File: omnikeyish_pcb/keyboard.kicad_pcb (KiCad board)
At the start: 2 copper layers, 485.9 x 139.8 mm, 344 parts, among them SW1.1 KEY_P11, SW1.10 KEY_F6, SW1.11 KEY_F7, SW1.12 KEY_F8, SW1.13 KEY_F9, SW1.14 KEY_F10, SW1.15 KEY_F11, SW1.16 KEY_F12, SW1.17 KEY_PRINTSCREEN, SW1.18 KEY_SCROLL_LOCK, SW1.19 KEY_PAUSE, SW1.2 KEY_P12, SW1.20 KEY_VOLMUTE, SW1.21 KEY_VOLDOWN, SW1.22 KEY_VOLUP, SW1.23 KEY_POWER, SW1.3 KEY_ESCAPE, SW1.5 KEY_F1, SW1.6 KEY_F2, SW1.7 KEY_F3, SW1.8 KEY_F4, SW1.9 KEY_F5, SW1B.1 KEY_P11, SW1B.10 KEY_F6, SW1B.11 KEY_F7, SW1B.12 KEY_F8, SW1B.13 KEY_F9, SW1B.14 KEY_F10, SW1B.15 KEY_F11, SW1B.16 KEY_F12, SW1B.17 KEY_PRINTSCREEN, SW1B.18 KEY_SCROLL_LOCK, SW1B.19 KEY_PAUSE, SW1B.2 KEY_P12, SW1B.3 KEY_ESCAPE, SW1B.5 KEY_F1, SW1B.6 KEY_F2, SW1B.7 KEY_F3, SW1B.8 KEY_F4, SW1B.9 KEY_F5, SW1C.1 KEY_P11, SW1C.2 KEY_P12, SW1D.1 KEY_P11, SW1D.2 KEY_P12, SW2.1 KEY_P1, SW2.10 KEY_7, SW2.11 KEY_8, SW2.12 KEY_9, SW2.13 KEY_0, SW2.14 KEY_MINUS, SW2.15 KEY_EQUALS, SW2.16 KEY_BACKSPACE, SW2.17 KEY_INSERT, SW2.18 KEY_HOME, SW2.19 KEY_PGUP, SW2.2 KEY_P2, SW2.20 KEY_NUMLOCK, SW2.21 KEY_NUMDIVIDE, SW2.22 KEY_NUMTIMES, SW2.23 KEY_NUMMINUS, SW2.3 KEY_BACKQUOTE, SW2.4 KEY_1, SW2.5 KEY_2, SW2.6 KEY_3, SW2.7 KEY_4, SW2.8 KEY_5, SW2.9 KEY_6, SW2B.1 KEY_P1, SW2B.17 KEY_BIGINSERT, SW2B.2 KEY_P2, SW2C.1 KEY_P1, SW2C.2 KEY_P2, SW3.1 KEY_P3, SW3.10 KEY_U, SW3.11 KEY_I, SW3.12 KEY_O, SW3.13 KEY_P, SW3.14 KEY_LEFTBRACKET, SW3.15 KEY_RIGHTBRACKET, SW3.16 KEY_ANSIBACKSLASH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

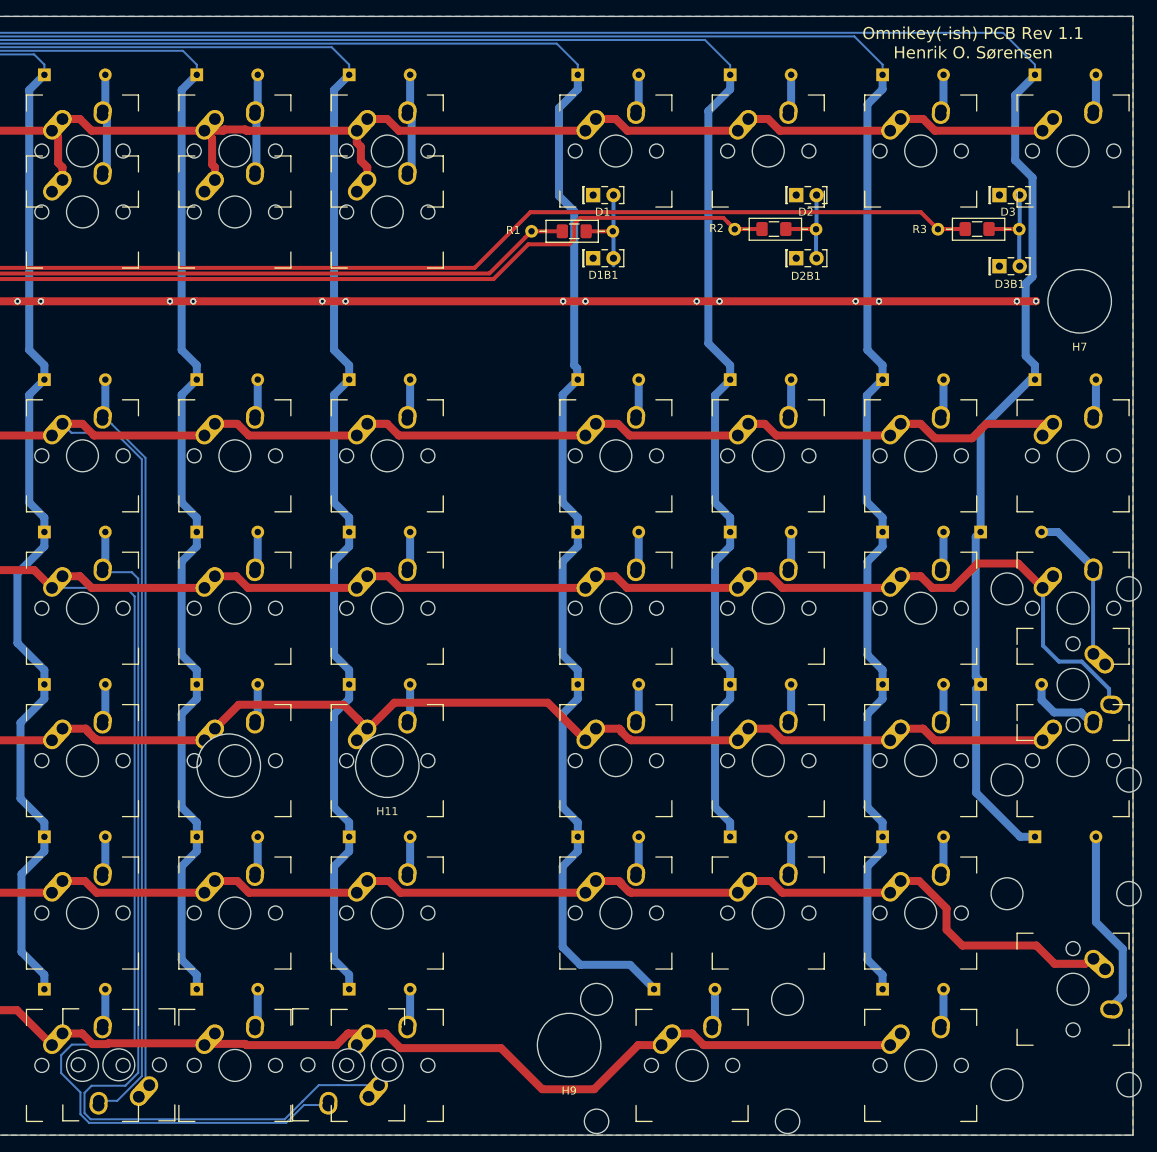
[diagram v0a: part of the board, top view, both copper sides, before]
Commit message: Rev 1.2: Fix brainfart matrix postion for Ultra's 1.5u insert and delete keys was wrong
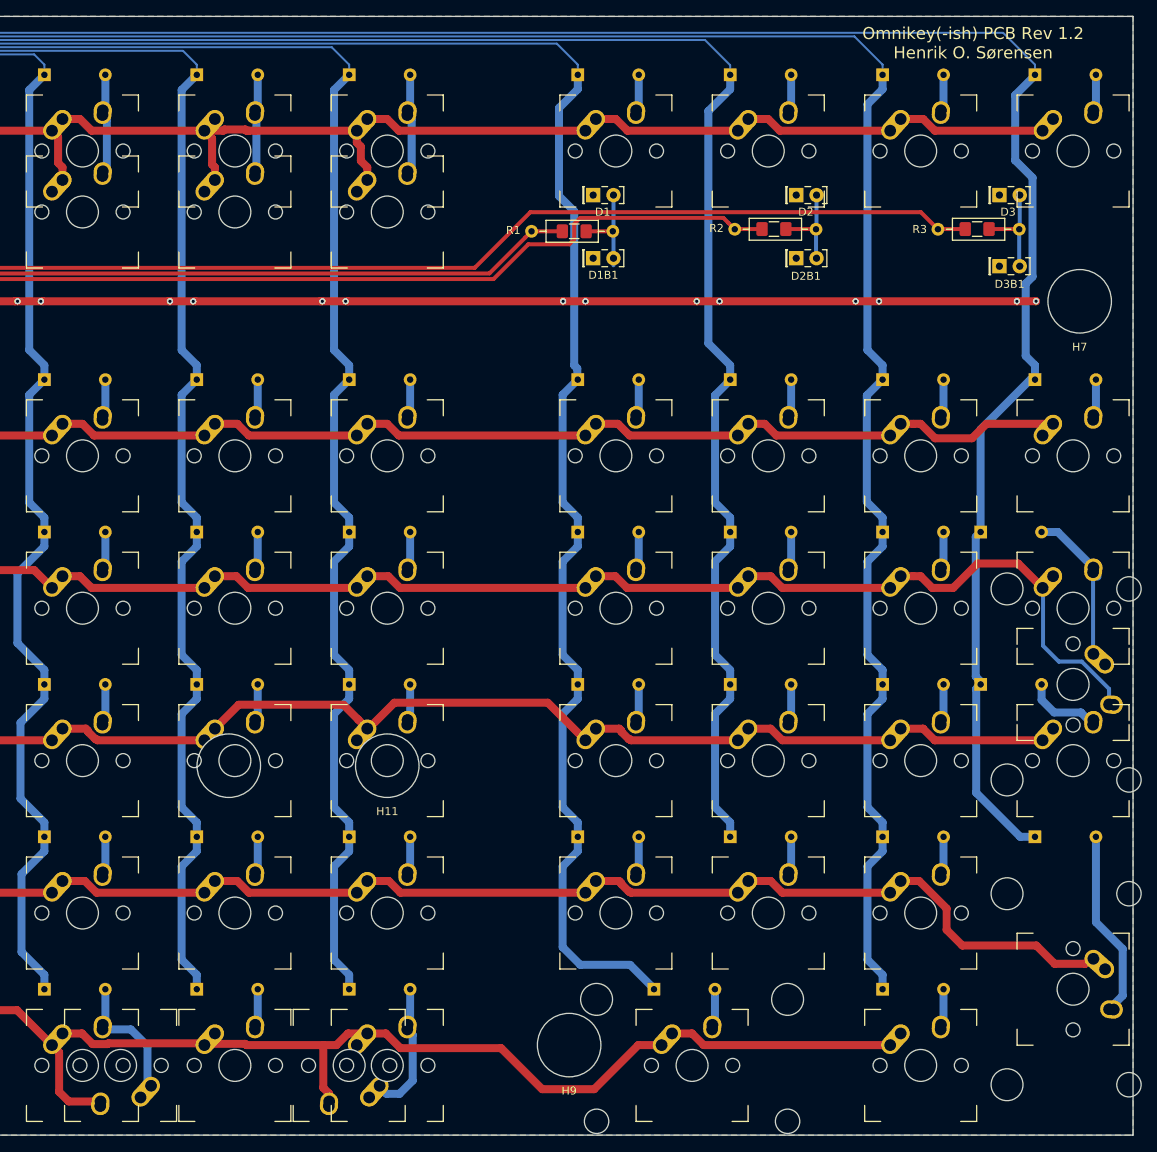
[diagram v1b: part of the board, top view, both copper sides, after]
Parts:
- removed SW2B.17: KEY_BIGINSERT, MX_Alps_Hybrid:MX-1.5U-NoLED
- removed SW3B.17: KEY_BIGDELETE, MX_Alps_Hybrid:MX-1.5U-NoLED
- added SW6B.17: KEY_ULTRAINSERT, MX_Alps_Hybrid:MX-1.5U-NoLED, F.Cu at (427.8, 174.0)
- added SW6B.19: KEY_ULTRADELETE, MX_Alps_Hybrid:MX-1.5U-NoLED, F.Cu at (456.4, 174.0)
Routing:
- net ROW3: track 786.9 -> 669.9 mm
- net Net-(D3.17-Pad2): track 120.4 -> 4.67 mm
- net ROW2: track 718.5 -> 623.0 mm
- net Net-(D2.17-Pad2): track 92.4 -> 4.67 mm
- net ROW6: track 767.6 -> 787.4 mm
- net Net-(D6.19-Pad2): track 5.17 -> 17.0 mm
- net Net-(D6.17-Pad2): track 5.17 -> 16.8 mm
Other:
- board text added: "Omnikey(-ish) PCB Rev 1.2 Henrik O. Sørensen"
- board text removed: "Omnikey(-ish) PCB Rev 1.1 Henrik O. Sørensen"

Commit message: Tweak silk screen location of 2u numpad plus
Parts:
- moved D4.23 0.65 mm to (534.7, 126.2)
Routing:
- net Net-(D4.3-Pad2): track 33.8 -> 29.6 mm
- net COL3: track 323.2 -> 324.2 mm
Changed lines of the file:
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@@
     (thickness 1.6)
     (drawings 50)
-    (tracks 2474)
+    (tracks 2473)
     (zones 0)
     (modules 344)
@@
   (module MX_Alps_Hybrid:MX-1.5U-NoLED (layer F.Cu)
     (at 456.3745 173.99 180)
-    (fp_text reference SW6B.19 (at 0 3.175) (layer B.SilkS)
+    (fp_text reference SW6B.19 (at -1.9685 -6.477) (layer B.SilkS)
       (effects (font (size 1 1) (thickness 0.15)) (justify mirror))
     )
@@
   (module MX_Alps_Hybrid:MX-1.5U-NoLED (layer F.Cu)
     (at 427.7995 173.99 180)
-    (fp_text reference SW6B.17 (at 0 3.175) (layer B.SilkS)
+    (fp_text reference SW6B.17 (at -2.8575 -6.35) (layer B.SilkS)
       (effects (font (size 1 1) (thickness 0.15)) (justify mirror))
     )
@@
   (module MX_Alps_Hybrid:MX-2U-NoLED (layer F.Cu)
     (at 546.862 126.365 270)
-    (fp_text reference SW3B.23 (at -1.7 -6.5 270) (layer B.SilkS)
+    (fp_text reference SW3B.23 (at -1.651 -6.35 270) (layer B.SilkS)
       (effects (font (size 1 1) (thickness 0.15)) (justify mirror))
     )
-    (fp_text value KEY_NUMBIGPLUS (at -0.2 -8.175 270) (layer B.SilkS)
+    (fp_text value KEY_NUMBIGPLUS (at -0.762 6.731 90) (layer B.SilkS)
       (effects (font (size 1 1) (thickness 0.15)) (justify mirror))
     )
@@
   )
   (module Diode_THT:D_DO-35_SOD27_P7.62mm_Horizontal (layer B.Cu)
-    (at 535.305 126.365)
+    (at 534.67 126.238)
     (descr "Diode, DO-35_SOD27 series, Axial, Horizontal, pin pitch=7.62mm, , length*diameter=4*2mm^2, , http://www.diodes.com/_files/packages/DO-35.pdf")
     (tags "Diode DO-35_SOD27 series Axial Horizontal pin pitch 7.62mm  length 4mm diameter 2mm")
-    (fp_text reference D4.23 (at 4.191 -2.286) (layer B.SilkS)
+    (fp_text reference D4.23 (at -2.032 0.127 90) (layer B.SilkS)
       (effects (font (size 1 1) (thickness 0.15)) (justify mirror))
     )
@@
   (module MX_Alps_Hybrid:MX-1U-NoLED (layer F.Cu)
     (at 546.862 116.84)
-    (fp_text reference SW3.23 (at -0.05 -7.075) (layer B.SilkS)
+    (fp_text reference SW3.23 (at 0 -8.636) (layer B.SilkS)
       (effects (font (size 1 1) (thickness 0.15)) (justify mirror))
     )
-    (fp_text value KEY_NUMPLUS (at 0 2.875) (layer B.SilkS)
+    (fp_text value KEY_NUMPLUS (at -0.381 -7.112) (layer B.SilkS)
       (effects (font (size 1 1) (thickness 0.15)) (justify mirror))
     )
@@
   (segment (start 126.873 145.415) (end 122.301 149.987) (width 1) (layer B.Cu) (net 21))
   (segment (start 127.762 145.415) (end 126.873 145.415) (width 1) (layer B.Cu) (net 21))
-  (segment (start 122.9995 140.6525) (end 127.762 145.415) (width 1) (layer B.Cu) (net 21))
-  (segment (start 122.9995 131.1275) (end 122.9995 140.6525) (width 1) (layer B.Cu) (net 21))
-  (segment (start 127.762 126.365) (end 122.9995 131.1275) (width 1) (layer B.Cu) (net 21))
   (segment (start 124.194978 46.747022) (end 120.777 50.165) (width 0.25) (layer F.Cu) (net 21))
   (segment (start 279.146 71.755) (end 280.242033 70.658967) (width 0.25) (layer F.Cu) (net 21))
@@
   (segment (start 280.242033 49.221979) (end 277.767076 46.747022) (width 0.25) (layer F.Cu) (net 21))
   (segment (start 277.767076 46.747022) (end 124.194978 46.747022) (width 0.25) (layer F.Cu) (net 21))
+  (segment (start 121.793 139.446) (end 127.762 145.415) (width 1) (layer B.Cu) (net 21))
+  (segment (start 121.793 132.334) (end 121.793 139.446) (width 1) (layer B.Cu) (net 21))
+  (segment (start 127.762 126.365) (end 121.793 132.334) (width 1) (layer B.Cu) (net 21))
   (segment (start 225.8695 50.165) (end 225.8695 54.8325) (width 1) (layer B.Cu) (net 22))
   (segment (start 209.931 62.23) (end 206.502 62.23) (width 1) (layer B.Cu) (net 22))
@@
   (segment (start 72.1995 90.065) (end 70.0405 92.224) (width 1) (layer B.Cu) (net 24))
   (segment (start 72.1995 88.265) (end 72.1995 90.065) (width 1) (layer B.Cu) (net 24))
-  (segment (start 70.0405 84.306) (end 72.1995 86.465) (width 1) (layer B.Cu) (net 24))
-  (segment (start 70.0405 54.124) (end 70.0405 84.306) (width 1) (layer B.Cu) (net 24))
-  (segment (start 72.1995 51.965) (end 70.0405 54.124) (width 1) (layer B.Cu) (net 24))
+  (segment (start 69.596 83.8615) (end 72.1995 86.465) (width 1) (layer B.Cu) (net 24))
+  (segment (start 69.596 54.5685) (end 69.596 83.8615) (width 1) (layer B.Cu) (net 24))
+  (segment (start 72.1995 51.965) (end 69.596 54.5685) (width 1) (layer B.Cu) (net 24))
   (segment (start 72.1995 86.465) (end 72.1995 88.265) (width 1) (layer B.Cu) (net 24))
   (segment (start 72.1995 50.165) (end 72.1995 51.965) (width 1) (layer B.Cu) (net 24))
@@
   (segment (start 135.382 130.4925) (end 135.0645 130.81) (width 1) (layer B.Cu) (net 63))
   (segment (start 135.382 126.365) (end 135.382 130.4925) (width 1) (layer B.Cu) (net 63))
-  (segment (start 137.50075 130.865) (end 137.44575 130.81) (width 1) (layer B.Cu) (net 63))
-  (segment (start 139.237 130.865) (end 137.50075 130.865) (width 1) (layer B.Cu) (net 63))
-  (segment (start 138.037 141.865) (end 142.037 137.865) (width 1) (layer B.Cu) (net 63))
-  (segment (start 142.037 137.865) (end 142.037 133.665) (width 1) (layer B.Cu) (net 63))
-  (segment (start 142.037 133.665) (end 139.237 130.865) (width 1) (layer B.Cu) (net 63))
-  (segment (start 129.11825 141.865) (end 138.037 141.865) (width 1) (layer B.Cu) (net 63))
-  (segment (start 127.64325 140.39) (end 129.11825 141.865) (width 1) (layer B.Cu) (net 63))
+  (segment (start 133.939501 129.685001) (end 135.0645 130.81) (width 1) (layer B.Cu) (net 63))
+  (segment (start 128.632999 129.685001) (end 133.939501 129.685001) (width 1) (layer B.Cu) (net 63))
+  (segment (start 123.063 135.255) (end 128.632999 129.685001) (width 1) (layer B.Cu) (net 63))
+  (segment (start 123.063 136.906) (end 123.063 135.255) (width 1) (layer B.Cu) (net 63))
+  (segment (start 126.547 140.39) (end 123.063 136.906) (width 1) (layer B.Cu) (net 63))
+  (segment (start 127.64325 140.39) (end 126.547 140.39) (width 1) (layer B.Cu) (net 63))
   (segment (start 239.776 131.3665) (end 239.7995 131.39) (width 1) (layer B.Cu) (net 64))
   (segment (start 239.776 128.0795) (end 239.776 131.3665) (width 1) (layer B.Cu) (net 64))
@@
   (segment (start 325.975935 47.610998) (end 325.975935 72.296065) (width 0.25) (layer B.Cu) (net 112))
   (segment (start 542.0995 50.165) (end 542.0995 48.895) (width 0.25) (layer B.Cu) (net 112))
-  (segment (start 540.258 145.415) (end 542.0995 145.415) (width 1) (layer B.Cu) (net 112))
-  (segment (start 534.7462 139.9032) (end 540.258 145.415) (width 1) (layer B.Cu) (net 112))
-  (segment (start 534.7462 126.9238) (end 534.7462 139.9032) (width 1) (layer B.Cu) (net 112))
-  (segment (start 535.305 126.365) (end 534.7462 126.9238) (width 1) (layer B.Cu) (net 112))
-  (segment (start 534.6954 125.3744) (end 535.305 125.984) (width 1) (layer B.Cu) (net 112))
-  (segment (start 534.6954 107.9246) (end 534.6954 125.3744) (width 1) (layer B.Cu) (net 112))
-  (segment (start 535.305 107.315) (end 534.6954 107.9246) (width 1) (layer B.Cu) (net 112))
   (segment (start 540.937 85.3025) (end 542.0995 86.465) (width 1) (layer B.Cu) (net 112))
   (segment (start 541.794501 75.407499) (end 540.937 76.265) (width 1) (layer B.Cu) (net 112))
@@
   (segment (start 542.0995 50.2285) (end 539.623 52.705) (width 1) (layer B.Cu) (net 112))
   (segment (start 542.0995 50.165) (end 542.0995 50.2285) (width 1) (layer B.Cu) (net 112))
+  (segment (start 534.6954 126.2126) (end 534.67 126.238) (width 1) (layer B.Cu) (net 112))
+  (segment (start 534.6954 107.9246) (end 534.6954 126.2126) (width 1) (layer B.Cu) (net 112))
+  (segment (start 535.305 107.315) (end 534.6954 107.9246) (width 1) (layer B.Cu) (net 112))
+  (segment (start 534.7462 126.3142) (end 534.7462 139.9032) (width 1) (layer B.Cu) (net 112))
+  (segment (start 540.258 145.415) (end 542.0995 145.415) (width 1) (layer B.Cu) (net 112))
+  (segment (start 534.7462 139.9032) (end 540.258 145.415) (width 1) (layer B.Cu) (net 112))
+  (segment (start 534.67 126.238) (end 534.7462 126.3142) (width 1) (layer B.Cu) (net 112))
   (segment (start 437.3245 124.565) (end 437.3245 126.365) (width 1) (layer B.Cu) (net 113))
   (segment (start 435.431999 122.672499) (end 437.3245 124.565) (width 1) (layer B.Cu) (net 113))
@@
   (segment (start 530.6695 126.365) (end 530.6695 131.0325) (width 1) (layer B.Cu) (net 139))
   (segment (start 549.7195 131.0325) (end 549.362 131.39) (width 1) (layer B.Cu) (net 140))
-  (segment (start 544.499599 129.869999) (end 542.925 128.2954) (width 1) (layer B.Cu) (net 140))
-  (segment (start 542.925 128.2954) (end 542.925 126.365) (width 1) (layer B.Cu) (net 140))
+  (segment (start 542.29 127.6604) (end 542.29 126.238) (width 1) (layer B.Cu) (net 140))
+  (segment (start 544.499599 129.869999) (end 542.29 127.6604) (width 1) (layer B.Cu) (net 140))
   (segment (start 547.841999 129.869999) (end 544.499599 129.869999) (width 1) (layer B.Cu) (net 140))
   (segment (start 549.362 131.39) (end 547.841999 129.869999) (width 1) (layer B.Cu) (net 140))

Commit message: Nav cluster to Numpad cluster distance was off by 1/32 of an inch (0.7935mm).
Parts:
- moved H5 315.2 mm to (483.9, 171.4)
- moved H9 315.2 mm to (181.0, 84.1)
- moved H11 307.9 mm to (155.6, 174.6)
- moved H2 307.9 mm to (461.1, 136.5)
- moved H4 206.5 mm to (547.7, 78.5)
- moved SW1.22 0.79 mm to (527.0, 59.7)
- moved SW2.22 0.79 mm to (527.0, 97.8)
- moved SW3.22 0.79 mm to (527.0, 116.8)
- moved SW4.22 0.79 mm to (527.0, 135.9)
- moved SW5.22 0.79 mm to (527.0, 154.9)
- moved SW6.20 0.79 mm to (498.4, 174.0)
- moved SW6.22 0.79 mm to (527.0, 174.0)
- moved SW1.20 0.79 mm to (488.9, 59.7)
- moved SW1.21 0.79 mm to (508.0, 59.7)
- moved SW2.20 0.79 mm to (488.9, 97.8)
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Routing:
- net ROW2: track 623.0 -> 618.6 mm
- net COL22: track 366.3 -> 370.6 mm
- net ROW6: track 787.4 -> 783.3 mm
- net COL20: track 341.1 -> 345.0 mm
- net COL21: track 329.7 -> 332.7 mm
- net ROW3: track 669.9 -> 672.3 mm
- net Net-(D4.23-Pad2): track 10.5 -> 9.06 mm
- net COL17: track 277.1 -> 275.7 mm
- net COL19: track 307.1 -> 307.9 mm
- net COL18: track 290.6 -> 291.2 mm
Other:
- board text added: "Omnikey(-ish) PCB Rev 1.3 Henrik O. Sørensen"
- board text removed: "Omnikey(-ish) PCB Rev 1.2 Henrik O. Sørensen"
